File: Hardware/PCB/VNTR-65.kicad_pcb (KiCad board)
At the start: 4 copper layers, 400 x 150 mm, 126 parts, among them J1 USB_C_Receptacle, J4 SM03B-SRSS-TB, SW1 SW_Push, SW2 SW_Push, SW3 RotaryEncoder, U1 RP2350_80QFN, U10 SW_MX_HE, U11 SW_MX_HE, U12 SW_MX_HE, U13 SW_MX_HE, U14 SW_MX_HE, U15 SW_MX_HE, U16 SW_MX_HE, U17 SW_MX_HE, U18 SW_MX_HE, U19 SW_MX_HE, U2 NCP1117-3.3_SOT223, U20 SW_MX_HE, U21 SW_MX_HE, U22 SW_MX_HE, U23 SW_MX_HE, U24 SW_MX_HE, U25 SW_MX_HE, U26 SW_MX_HE, U27 SW_MX_HE, U28 SW_MX_HE, U29 SW_MX_HE, U30 SW_MX_HE, U31 SW_MX_HE, U32 SW_MX_HE, U33 SW_MX_HE, U34 SW_MX_HE, U35 SW_MX_HE, U36 SW_MX_HE, U37 SW_MX_HE, U38 SW_MX_HE, U39 SW_MX_HE, U4 CH221K, U40 SW_MX_HE, U41 SW_MX_HE, U42 SW_MX_HE, U43 SW_MX_HE, U44 SW_MX_HE, U45 SW_MX_HE, U46 SW_MX_HE, U47 SW_MX_HE, U48 SW_MX_HE, U49 SW_MX_HE, U5 CD74HC4067M, U50 SW_MX_HE, U51 SW_MX_HE, U52 SW_MX_HE, U53 SW_MX_HE, U54 SW_MX_HE, U55 SW_MX_HE, U56 SW_MX_HE, U57 SW_MX_HE, U58 SW_MX_HE, U59 SW_MX_HE, U6 CD74HC4067M, U60 SW_MX_HE, U61 SW_MX_HE, U62 SW_MX_HE, U63 SW_MX_HE, U64 SW_MX_HE, U65 SW_MX_HE, U66 SW_MX_HE, U67 SW_MX_HE, U68 SW_MX_HE, U69 SW_MX_HE, U7 CD74HC4067M, U70 SW_MX_HE, U71 SW_MX_HE, U72 SW_MX_HE, U73 SW_MX_HE, U74 SW_MX_HE, U75 SW_MX_HE, U76 SW_MX_HE, U78 ER_OLEDM0.91_1x-I2C, U8 CD74HC4067M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

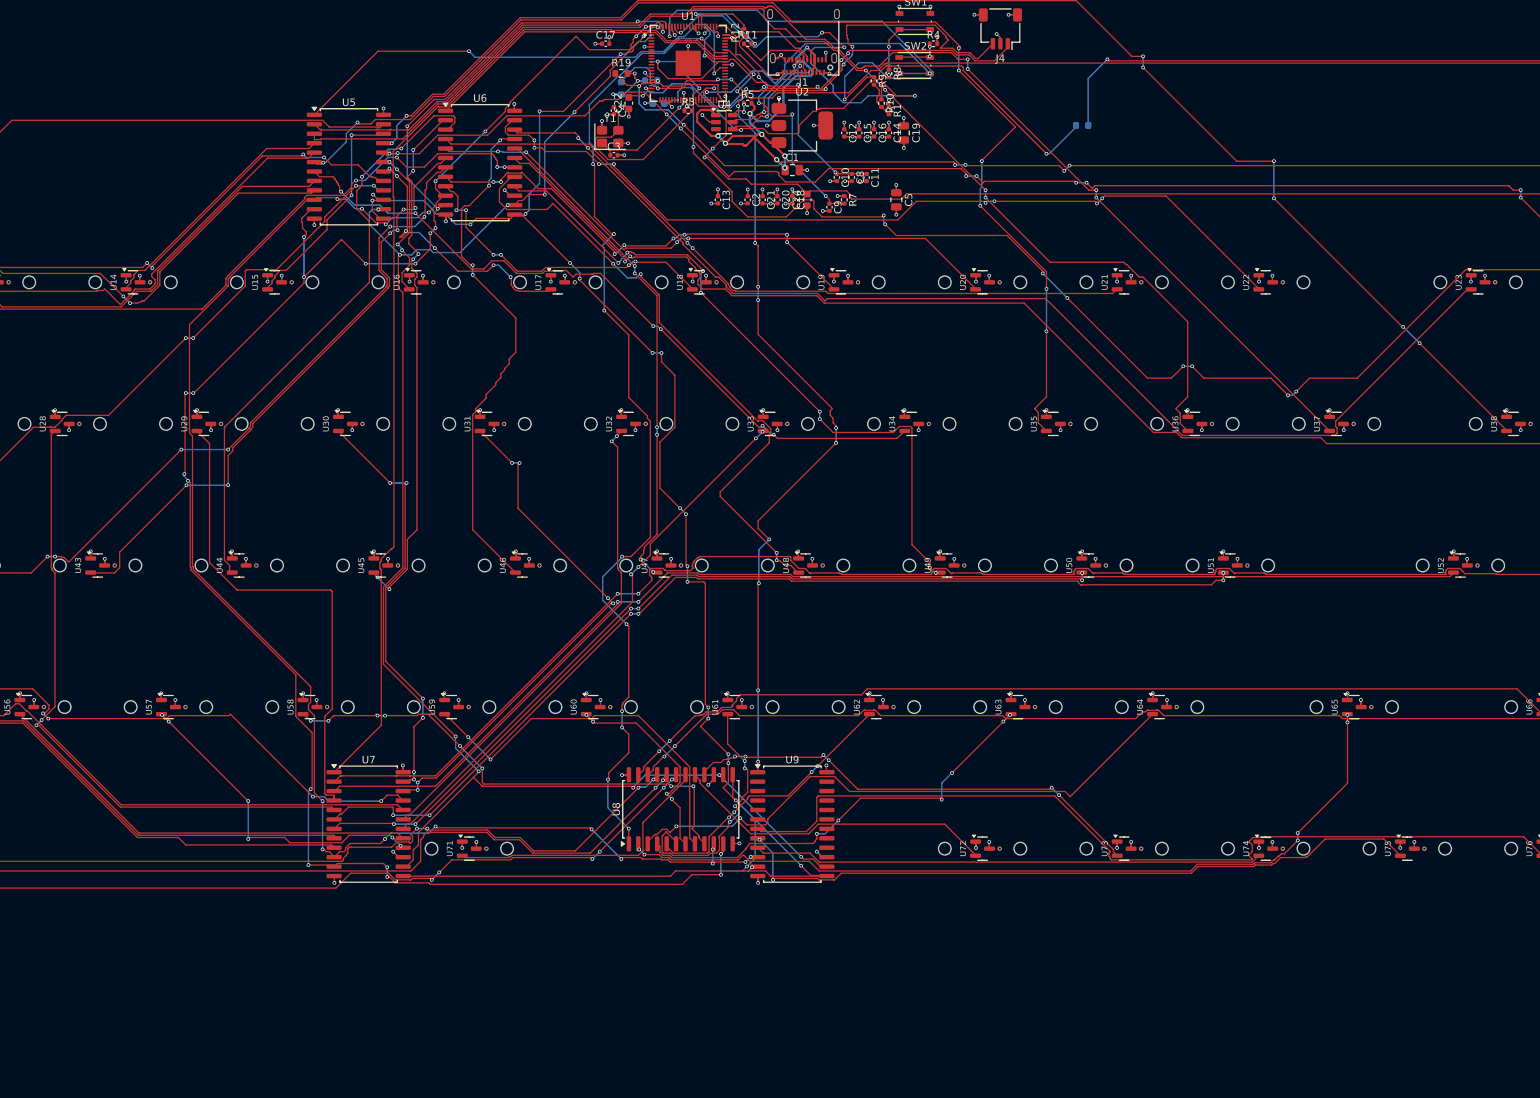
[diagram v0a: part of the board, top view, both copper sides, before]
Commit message: added more mounting holes
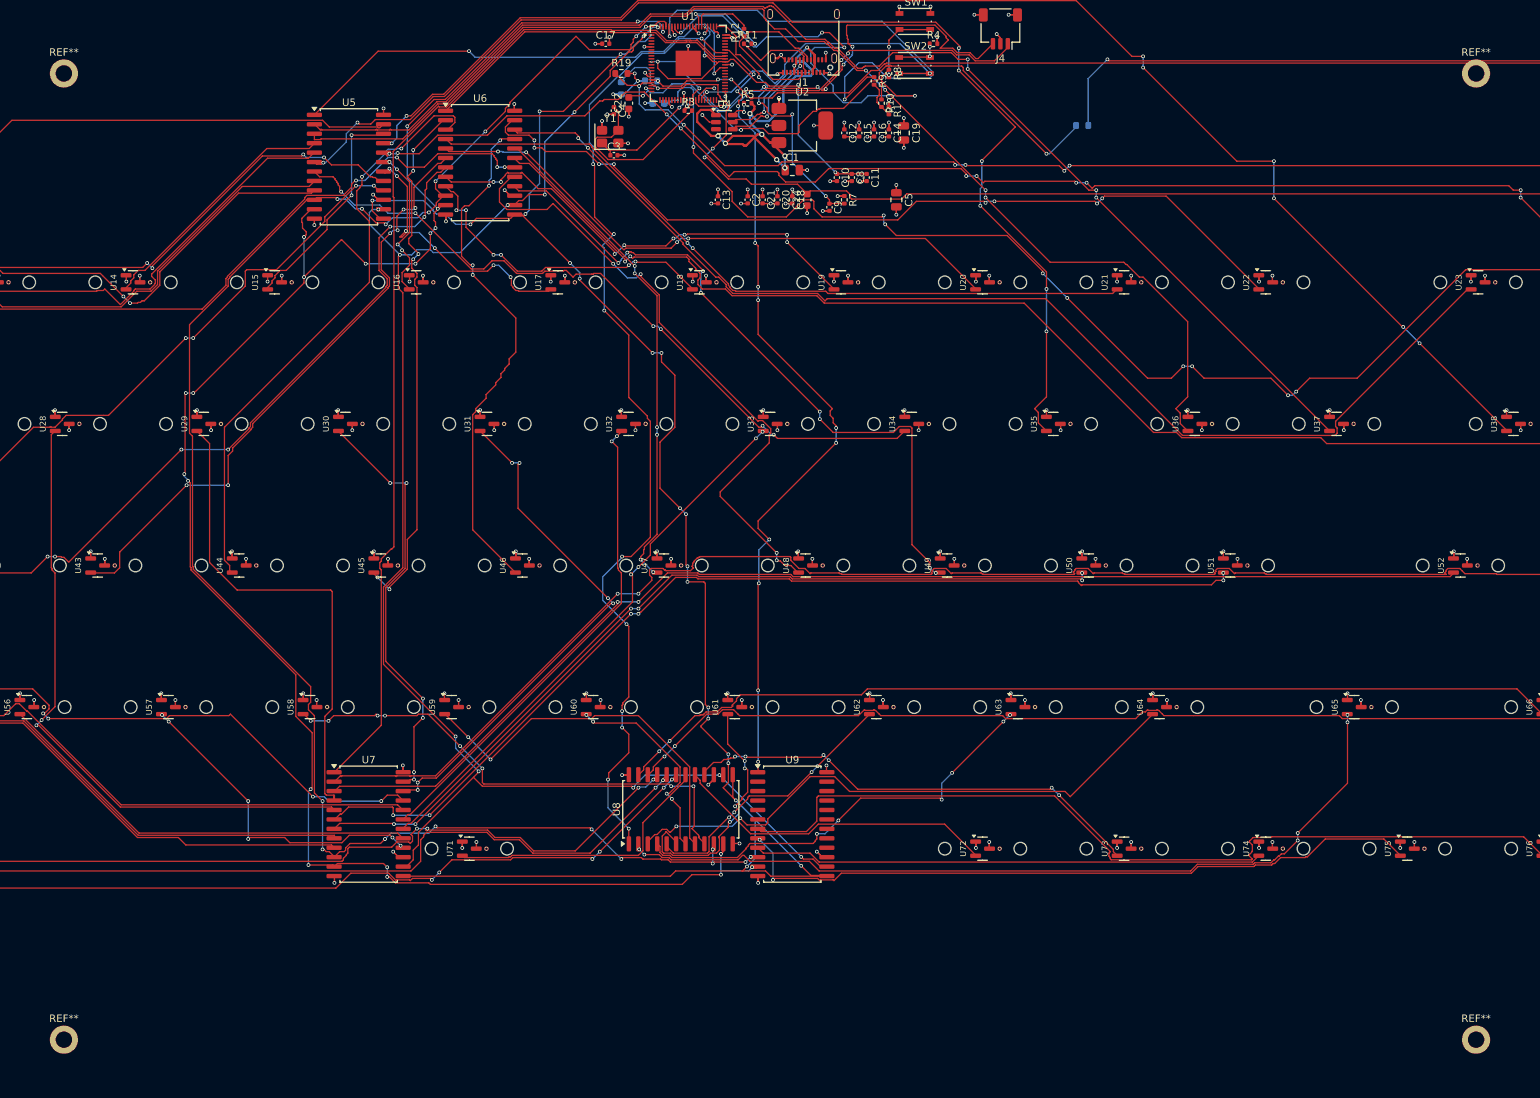
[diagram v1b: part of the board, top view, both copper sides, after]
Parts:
- added REF**: MountingHole_2.2mm_M2_DIN965_Pad, MountingHole:MountingHole_2.2mm_M2_DIN965_Pad, F.Cu at (105.0, 140.0)
- added REF**: MountingHole_2.2mm_M2_DIN965_Pad, MountingHole:MountingHole_2.2mm_M2_DIN965_Pad, F.Cu at (295.0, 10.0)
- added REF**: MountingHole_2.2mm_M2_DIN965_Pad, MountingHole:MountingHole_2.2mm_M2_DIN965_Pad, F.Cu at (105.0, 10.0)
- added REF**: MountingHole_2.2mm_M2_DIN965_Pad, MountingHole:MountingHole_2.2mm_M2_DIN965_Pad, F.Cu at (295.0, 140.0)

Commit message: Refined the pcb design overall
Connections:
- R15 pad 2: +3.3V -> +3V3
- R16 pad 1: +3.3V -> +3V3
- R19 pad 2: +3.3V -> +3V3
- RV1 pad 1: +3.3V -> +3V3
- U10 pad 1: +3.3V -> +3V3
- U11 pad 1: +3.3V -> +3V3
- U12 pad 1: +3.3V -> +3V3
- U13 pad 1: +3.3V -> +3V3
- U14 pad 1: +3.3V -> +3V3
- U15 pad 1: +3.3V -> +3V3
- U16 pad 1: +3.3V -> +3V3
- U17 pad 1: +3.3V -> +3V3
- U18 pad 1: +3.3V -> +3V3
- U19 pad 1: +3.3V -> +3V3
- U20 pad 1: +3.3V -> +3V3
- U21 pad 1: +3.3V -> +3V3
- U22 pad 1: +3.3V -> +3V3
- U23 pad 1: +3.3V -> +3V3
- U24 pad 1: +3.3V -> +3V3
- U25 pad 1: +3.3V -> +3V3
- U26 pad 1: +3.3V -> +3V3
- U27 pad 1: +3.3V -> +3V3
- U28 pad 1: +3.3V -> +3V3
- U29 pad 1: +3.3V -> +3V3
- U30 pad 1: +3.3V -> +3V3
- U31 pad 1: +3.3V -> +3V3
- U32 pad 1: +3.3V -> +3V3
- U33 pad 1: +3.3V -> +3V3
- U34 pad 1: +3.3V -> +3V3
- U35 pad 1: +3.3V -> +3V3
- U36 pad 1: +3.3V -> +3V3
- U37 pad 1: +3.3V -> +3V3
- U38 pad 1: +3.3V -> +3V3
- U39 pad 1: +3.3V -> +3V3
- U40 pad 1: +3.3V -> +3V3
- U41 pad 1: +3.3V -> +3V3
- U42 pad 1: +3.3V -> +3V3
- U43 pad 1: +3.3V -> +3V3
- U44 pad 1: +3.3V -> +3V3
- U45 pad 1: +3.3V -> +3V3
- U46 pad 1: +3.3V -> +3V3
- U47 pad 1: +3.3V -> +3V3
- U48 pad 1: +3.3V -> +3V3
- U49 pad 1: +3.3V -> +3V3
- U5 pad 24: +3.3V -> +3V3
- U50 pad 1: +3.3V -> +3V3
- U51 pad 1: +3.3V -> +3V3
- U52 pad 1: +3.3V -> +3V3
- U53 pad 1: +3.3V -> +3V3
- U54 pad 1: +3.3V -> +3V3
- U55 pad 1: +3.3V -> +3V3
- U56 pad 1: +3.3V -> +3V3
- U57 pad 1: +3.3V -> +3V3
- U58 pad 1: +3.3V -> +3V3
- U59 pad 1: +3.3V -> +3V3
- U6 pad 24: +3.3V -> +3V3
- U60 pad 1: +3.3V -> +3V3
- U61 pad 1: +3.3V -> +3V3
- U62 pad 1: +3.3V -> +3V3
- U63 pad 1: +3.3V -> +3V3
- U64 pad 1: +3.3V -> +3V3
- U65 pad 1: +3.3V -> +3V3
- U66 pad 1: +3.3V -> +3V3
- U67 pad 1: +3.3V -> +3V3
- U68 pad 1: +3.3V -> +3V3
- U69 pad 1: +3.3V -> +3V3
- U7 pad 24: +3.3V -> +3V3
- U70 pad 1: +3.3V -> +3V3
- U71 pad 1: +3.3V -> +3V3
- U72 pad 1: +3.3V -> +3V3
- U73 pad 1: +3.3V -> +3V3
- U74 pad 1: +3.3V -> +3V3
- U75 pad 1: +3.3V -> +3V3
- U76 pad 1: +3.3V -> +3V3
- U8 pad 24: +3.3V -> +3V3
- U9 pad 24: +3.3V -> +3V3
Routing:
- net +3.3V: track 74.0 -> 0.00 mm, vias 75 -> 0
- net +3V3: track 29.0 -> 102.5 mm, vias 26 -> 100
- net Net-(R14-Pad2): track 148.1 -> 152.9 mm
- net /GPIO16: track 154.5 -> 157.4 mm
- net VBUS: track 66.0 -> 64.6 mm
- net +1V1: track 58.6 -> 58.4 mm, vias 7 -> 6
- net GND: vias 114 -> 47
- removed copper zone on In2.Cu, net +3.3V

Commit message: Reduced case volume and centered USB-C on PCB
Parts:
- moved REF** 4.51 mm to (109.5, 140.0)
- moved REF** 4.51 mm to (109.5, 10.0)
- moved REF** 4.51 mm to (14.5, 10.0)
- moved REF** 4.51 mm to (299.5, 10.0)
- moved REF** 4.51 mm to (394.5, 10.0)
- moved REF** 4.51 mm to (299.5, 140.0)
- moved REF** 4.51 mm to (394.5, 140.0)

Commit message: Update pcb to smaller size
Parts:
- added U77: SW_MX_HE, PCM_marbastlib-he:SW_MX_HE_0deg_1u, F.Cu at (299.3, 108.8)
- moved U7 211.5 mm to (353.9, 71.8)
- moved U9 150.2 mm to (352.5, 96.5)
- moved U8 136.8 mm to (324.8, 111.2)
- moved REF** 61.8 mm to (244.2, 112.5)
- moved REF** 55.5 mm to (244.2, 5.50)
- moved REF** 50.2 mm to (352.5, 112.5)
- moved C13 48.1 mm to (145.3, 21.0)
- moved C18 48.1 mm to (155.3, 21.0)
- moved C2 48.1 mm to (149.3, 21.0)
- moved C20 48.1 mm to (153.3, 21.0)
- moved C21 48.1 mm to (151.3, 21.0)
- moved C24 48.1 mm to (157.3, 21.0)
- moved C5 48.1 mm to (169.3, 21.0)
- moved C9 48.1 mm to (160.3, 22.0)
- moved R7 48.1 mm to (162.3, 21.0)
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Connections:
- U9 pad 6: unconnected-(U9-I3-Pad6) -> Net-(U77-VOUT)
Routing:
- net GPIO2: track 255.4 -> 0.00 mm, vias 21 -> 0
- net GPIO4: track 244.8 -> 0.00 mm, vias 21 -> 0
- net GPIO1: track 235.6 -> 0.00 mm, vias 18 -> 0
- net Net-(U53-VOUT): track 212.1 -> 0.00 mm, vias 2 -> 0
- net GPIO3: track 210.8 -> 0.00 mm, vias 12 -> 0
- net Net-(U39-VOUT): track 210.7 -> 0.00 mm, vias 10 -> 0
- net /GPIO26: track 194.0 -> 0.00 mm, vias 11 -> 0
- net Net-(U24-VOUT): track 193.9 -> 0.00 mm, vias 4 -> 0
- net Net-(U38-VOUT): track 187.8 -> 0.00 mm, vias 8 -> 0
- net /GPIO18: track 184.1 -> 0.00 mm, vias 4 -> 0
- net Net-(U37-VOUT): track 171.1 -> 0.00 mm, vias 4 -> 0
- net Net-(U52-VOUT): track 163.5 -> 0.00 mm, vias 2 -> 0
- net Net-(U35-VOUT): track 161.0 -> 0.00 mm, vias 8 -> 0
- net Net-(U36-VOUT): track 160.3 -> 0.00 mm, vias 4 -> 0
- net /GPIO17: track 160.2 -> 0.00 mm, vias 6 -> 0
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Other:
- board size 400 x 150 mm -> 370 x 120 mm
